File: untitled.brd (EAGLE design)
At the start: 59.4 x 57.8 mm, 25 parts

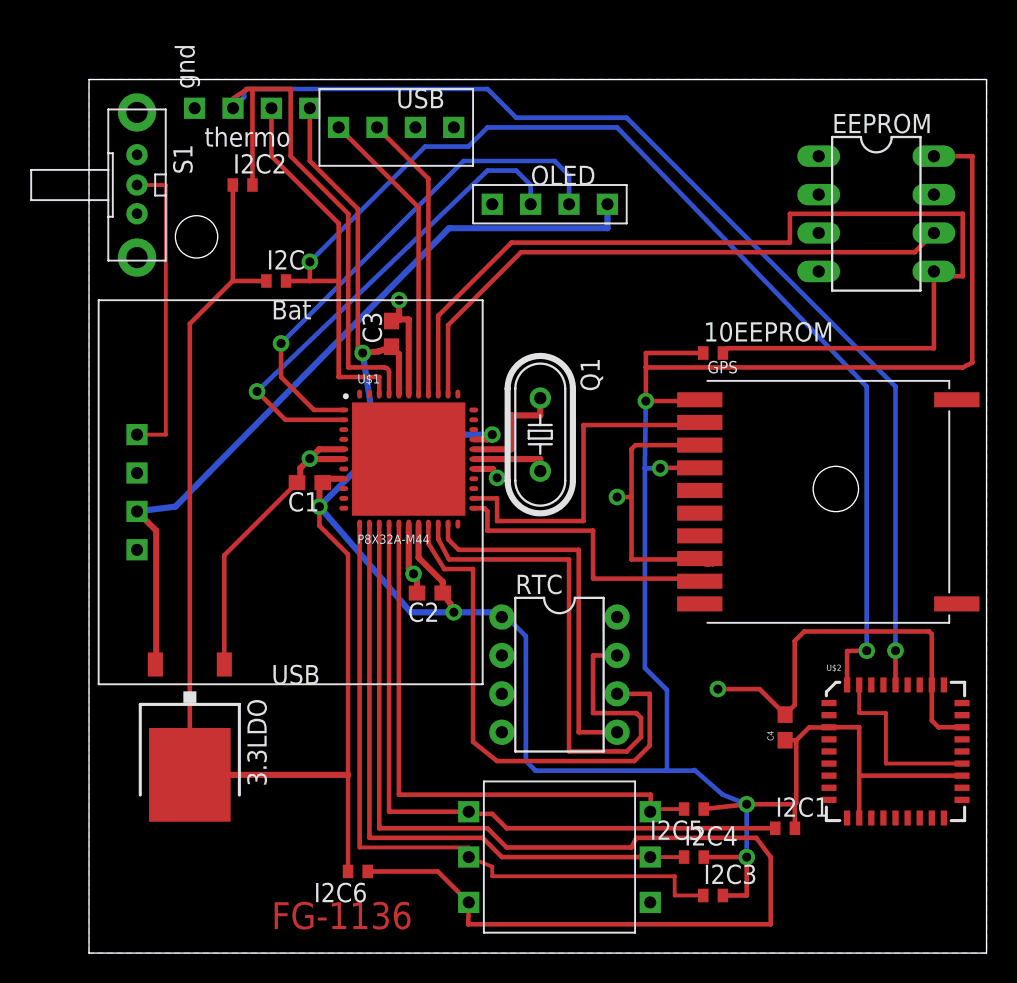
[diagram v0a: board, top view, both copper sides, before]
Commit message: Shrunk board form factor
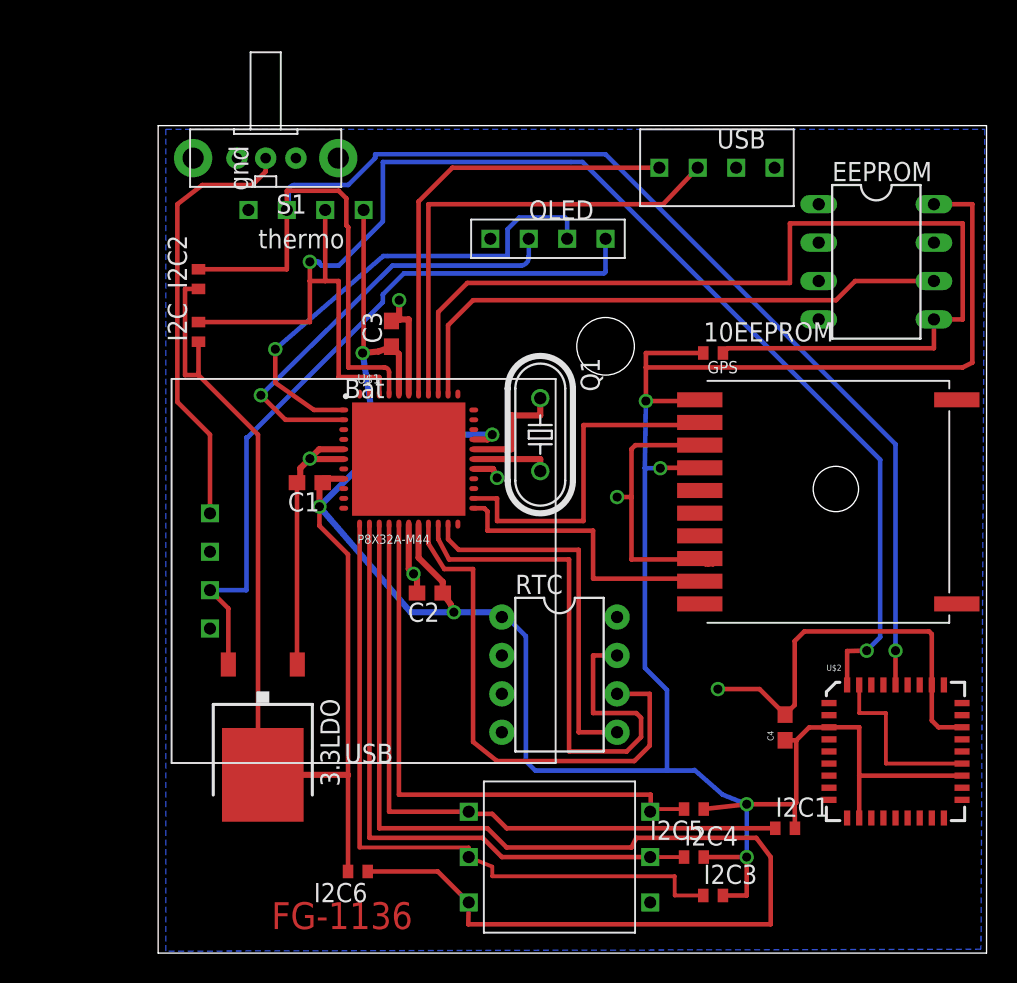
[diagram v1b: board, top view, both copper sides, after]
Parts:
- moved USB 21.4 mm to (75.2, 62.1)
- moved S1 8.69 mm to (45.3, 62.7), turned to 180 degrees
- moved THERMO 7.61 mm to (46.7, 59.3)
- moved LIPOCHARGER-BOOSTER 7.10 mm to (46.7, 36.7)
- moved I2C2 6.87 mm to (40.9, 54.7), turned to 90 degrees
- moved I2C 6.15 mm to (40.9, 51.2), turned to 90 degrees
- moved 3.3LDO 4.83 mm to (45.1, 24.4)
- moved EEPROM 3.17 mm to (85.7, 55.9)
- moved OLED_SCREEN 2.29 mm to (65.3, 57.4)
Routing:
- net +3V3: track 290.6 -> 270.1 mm
- net N$9: track 19.0 -> 31.4 mm
- net SCL: track 107.7 -> 97.2 mm
- net N$7: track 19.8 -> 29.6 mm
- net N$13: track 20.3 -> 28.9 mm
- net N$10: track 32.1 -> 28.8 mm
- net +5V: track 51.2 -> 48.7 mm
- net GND: track 82.1 -> 80.1 mm
- net N$19: track 39.2 -> 37.9 mm
- net N$11: track 33.6 -> 32.3 mm
- net SDA: track 97.0 -> 95.9 mm
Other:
- board size 59.4 x 57.8 mm -> 54.8 x 54.7 mm

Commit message: Made correction in hole size for through hole components
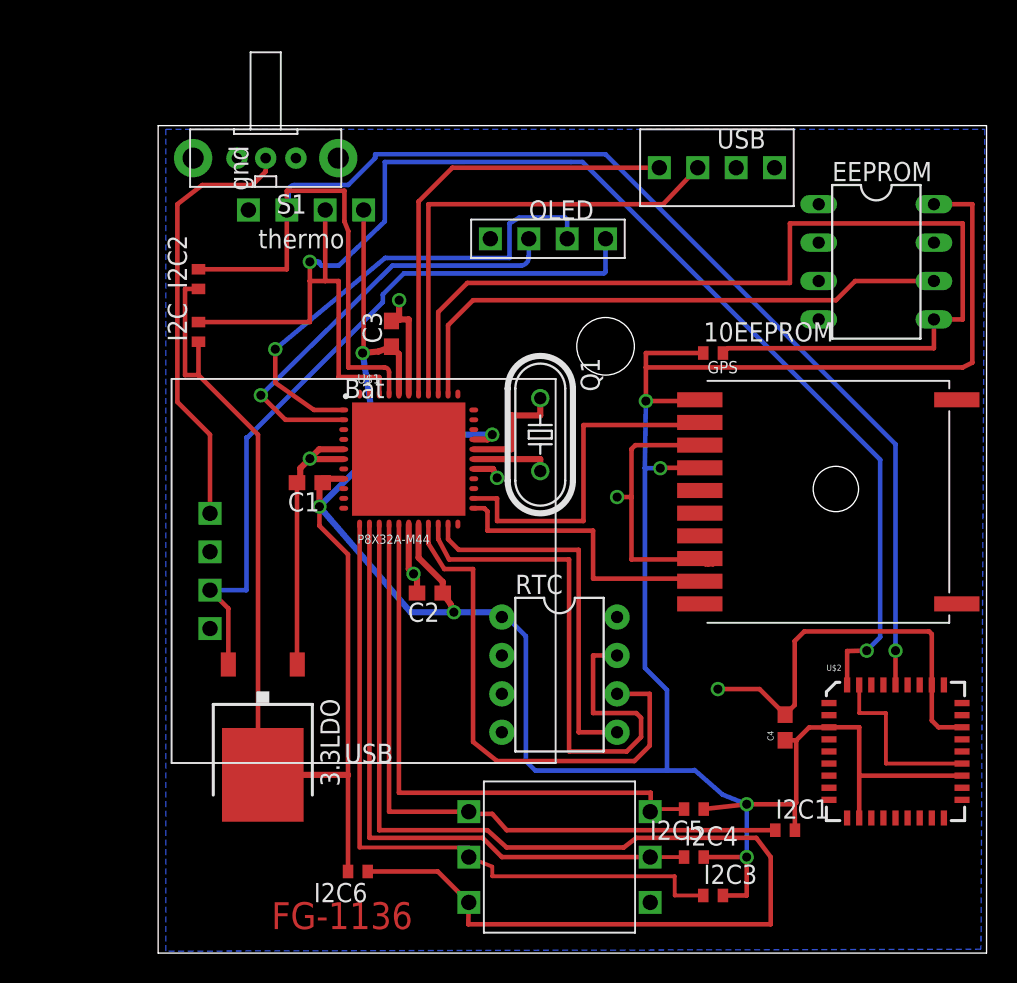
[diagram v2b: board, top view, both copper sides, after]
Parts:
- moved I2C1 0.13 mm to (79.7, 18.3)
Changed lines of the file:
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@@
 <element name="I2C3" library="adafruit" package="R1005" value="" x="74.93" y="13.97"/>
 <element name="I2C6" library="adafruit" package="R1005" value="" x="51.435" y="15.5575" rot="R180"/>
-<element name="I2C1" library="adafruit" package="R1005" value="" x="79.6925" y="18.415"/>
+<element name="I2C1" library="adafruit" package="R1005" value="" x="79.6925" y="18.288"/>
 <element name="U$2" library="SparkFun" package="LCC36" value="HMC6343A" x="86.995" y="23.495"/>
 <element name="C1" library="rcl" package="C0603" value="" x="48.26" y="41.275" rot="R180"/>
@@
 <wire x1="50.8" y1="48.895" x2="53.1825" y2="48.895" width="0.3048" layer="1"/>
 <wire x1="53.1825" y1="48.895" x2="53.5" y2="48.5775" width="0.3048" layer="1" curve="-90"/>
-<wire x1="50.165" y1="60.579" x2="46.736" y2="60.579" width="0.3048" layer="1"/>
+<wire x1="50.546" y1="60.579" x2="46.736" y2="60.579" width="0.3048" layer="1"/>
 <wire x1="46.736" y1="60.579" x2="46.736" y2="59.309" width="0.3048" layer="1"/>
 <wire x1="86.995" y1="43.815" x2="67.818" y2="62.992" width="0.3048" layer="16"/>
@@
 <wire x1="46.863" y1="60.579" x2="46.863" y2="59.436" width="0.3048" layer="16"/>
 <wire x1="46.863" y1="59.436" x2="46.736" y2="59.309" width="0.3048" layer="16" curve="-90"/>
-<wire x1="50.8" y1="48.895" x2="50.8" y2="58.166" width="0.3048" layer="1"/>
-<wire x1="50.8" y1="58.166" x2="50.673" y2="58.293" width="0.3048" layer="1"/>
-<wire x1="50.673" y1="58.293" x2="50.673" y2="60.071" width="0.3048" layer="1"/>
-<wire x1="50.165" y1="60.579" x2="50.673" y2="60.071" width="0.3048" layer="1"/>
+<wire x1="50.8" y1="48.895" x2="50.8" y2="57.912" width="0.3048" layer="1"/>
 <wire x1="40.894" y1="55.387" x2="46.736" y2="55.387" width="0.3048" layer="1"/>
 <wire x1="46.736" y1="55.387" x2="46.736" y2="59.309" width="0.3048" layer="1"/>
 <wire x1="86.995" y1="43.815" x2="86.995" y2="30.1625" width="0.3048" layer="16"/>
+<wire x1="50.546" y1="60.579" x2="50.546" y2="58.547" width="0.3048" layer="1"/>
+<wire x1="50.546" y1="58.547" x2="50.8" y2="57.912" width="0.3048" layer="1"/>
 </signal>
 <signal name="SDA">
@@
 <wire x1="83.795" y1="30.1375" x2="85.09" y2="30.1625" width="0.3048" layer="1"/>
 <via x="85.09" y="30.1625" extent="1-16" drill="0.6" shape="square"/>
-<wire x1="65.532" y1="62.484" x2="53.08980625" y2="62.4820625" width="0.3048" layer="16"/>
+<wire x1="65.532" y1="62.484" x2="53.21680625" y2="62.4820625" width="0.3048" layer="16"/>
 <via x="48.26" y="55.88" extent="1-16" drill="0.6" shape="square"/>
 <wire x1="48.26" y1="55.88" x2="48.26" y2="54.61" width="0.3048" layer="1"/>
@@
 <wire x1="65.532" y1="62.484" x2="66.294" y2="62.484" width="0.3048" layer="16"/>
 <wire x1="66.294" y1="62.484" x2="85.979" y2="42.799" width="0.3048" layer="16"/>
-<wire x1="53.08980625" y1="62.4820625" x2="53.08980625" y2="58.55080625" width="0.3048" layer="16"/>
-<wire x1="53.08980625" y1="58.55080625" x2="50.165" y2="55.626" width="0.3048" layer="16"/>
+<wire x1="53.21680625" y1="62.4820625" x2="53.21680625" y2="58.55080625" width="0.3048" layer="16"/>
+<wire x1="53.21680625" y1="58.55080625" x2="50.165" y2="55.626" width="0.3048" layer="16"/>
 <wire x1="50.165" y1="55.626" x2="49.022" y2="55.626" width="0.3048" layer="16"/>
 <wire x1="49.022" y1="55.626" x2="48.768" y2="55.88" width="0.3048" layer="16"/>
@@
 <contactref element="U$1" pad="1"/>
 <via x="45.974" y="50.1015" extent="1-16" drill="0.6" shape="square"/>
-<wire x1="53.11975" y1="56.2665625" x2="45.974" y2="50.1015" width="0.3048" layer="16"/>
+<wire x1="53.24675" y1="56.1395625" x2="45.974" y2="50.1015" width="0.3048" layer="16"/>
 <wire x1="50.5" y1="46.0813" x2="48.5337" y2="46.0813" width="0.3048" layer="1"/>
 <wire x1="48.5337" y1="46.0813" x2="45.974" y2="47.879" width="0.3048" layer="1"/>
@@
 <wire x1="65.278" y1="58.674" x2="65.151" y2="58.801" width="0.3048" layer="16"/>
 <wire x1="65.151" y1="58.801" x2="62.103" y2="58.801" width="0.3048" layer="16"/>
-<wire x1="62.103" y1="58.801" x2="61.341" y2="58.039" width="0.3048" layer="16"/>
-<wire x1="61.341" y1="58.039" x2="61.341" y2="56.261" width="0.3048" layer="16"/>
-<wire x1="61.341" y1="56.261" x2="53.3793125" y2="56.261" width="0.3048" layer="16"/>
-<wire x1="53.3793125" y1="56.261" x2="53.11975" y2="56.2665625" width="0.3048" layer="16"/>
+<wire x1="62.103" y1="58.801" x2="61.468" y2="58.42" width="0.3048" layer="16"/>
+<wire x1="61.468" y1="58.42" x2="61.468" y2="56.134" width="0.3048" layer="16"/>
+<wire x1="61.468" y1="56.134" x2="53.3793125" y2="56.134" width="0.3048" layer="16"/>
+<wire x1="53.3793125" y1="56.134" x2="53.24675" y2="56.1395625" width="0.3048" layer="16"/>
 </signal>
 <signal name="N$18">
@@
 <wire x1="53.5" y1="38.5313" x2="53.5" y2="19.51" width="0.3048" layer="1"/>
 <wire x1="53.5" y1="19.51" x2="58.77" y2="19.51" width="0.3048" layer="1"/>
-<wire x1="79.0425" y1="18.415" x2="61.2775" y2="18.415" width="0.3048" layer="1"/>
-<wire x1="61.2775" y1="18.415" x2="60.325" y2="19.3675" width="0.3048" layer="1"/>
+<wire x1="79.0425" y1="18.288" x2="61.2775" y2="18.288" width="0.3048" layer="1"/>
+<wire x1="61.2775" y1="18.288" x2="60.325" y2="19.3675" width="0.3048" layer="1"/>
 <wire x1="60.325" y1="19.3675" x2="58.9125" y2="19.3675" width="0.3048" layer="1"/>
 <wire x1="58.9125" y1="19.3675" x2="58.77" y2="19.51" width="0.3048" layer="1"/>
@@
 <contactref element="5WAYSWITCH" pad="D"/>
 <contactref element="I2C6" pad="1"/>
-<wire x1="52.85" y1="38.5313" x2="52.85" y2="18.415" width="0.3048" layer="1"/>
+<wire x1="52.85" y1="38.5313" x2="52.85" y2="18.288" width="0.3048" layer="1"/>
 <wire x1="77.7875" y1="17.78" x2="78.74" y2="16.51" width="0.3048" layer="1"/>
 <wire x1="78.74" y1="16.51" x2="78.74" y2="12.065" width="0.3048" layer="1"/>
 <wire x1="78.74" y1="12.065" x2="58.7375" y2="12.065" width="0.3048" layer="1"/>
 <wire x1="58.7375" y1="12.065" x2="58.77" y2="13.51" width="0.3048" layer="1"/>
-<wire x1="52.85" y1="18.415" x2="60.0075" y2="18.415" width="0.3048" layer="1"/>
-<wire x1="60.0075" y1="18.415" x2="61.2775" y2="17.145" width="0.3048" layer="1"/>
-<wire x1="61.2775" y1="17.145" x2="69.5325" y2="17.145" width="0.3048" layer="1"/>
+<wire x1="52.85" y1="18.288" x2="60.0075" y2="18.288" width="0.3048" layer="1"/>
+<wire x1="60.0075" y1="18.288" x2="61.2775" y2="17.145" width="0.3048" layer="1"/>
+<wire x1="61.2775" y1="17.145" x2="69.0245" y2="17.145" width="0.3048" layer="1"/>
 <wire x1="69.85" y1="17.78" x2="77.7875" y2="17.78" width="0.3048" layer="1"/>
 <wire x1="52.085" y1="15.5575" x2="56.7225" y2="15.5575" width="0.3048" layer="1"/>
 <wire x1="56.7225" y1="15.5575" x2="58.77" y2="13.51" width="0.3048" layer="1"/>
-<wire x1="69.85" y1="17.78" x2="69.5325" y2="17.145" width="0.3048" layer="1"/>
+<wire x1="69.85" y1="17.78" x2="69.0245" y2="17.145" width="0.3048" layer="1"/>
 </signal>
 <signal name="N$17">
@@
 <wire x1="73.01" y1="19.685" x2="70.77" y2="19.685" width="0.254" layer="1"/>
 <wire x1="70.77" y1="19.685" x2="70.77" y2="19.51" width="0.254" layer="1"/>
-<wire x1="54.15" y1="38.5313" x2="54.15" y2="20.6375" width="0.3048" layer="1"/>
-<wire x1="54.15" y1="20.6375" x2="70.8025" y2="20.6375" width="0.3048" layer="1"/>
-<wire x1="70.8025" y1="20.6375" x2="70.8025" y2="19.51" width="0.3048" layer="1"/>
+<wire x1="54.15" y1="38.5313" x2="54.15" y2="20.7645" width="0.3048" layer="1"/>
+<wire x1="54.15" y1="20.7645" x2="70.8025" y2="20.7645" width="0.3048" layer="1"/>
+<wire x1="70.8025" y1="20.7645" x2="70.8025" y2="19.51" width="0.3048" layer="1"/>
 <wire x1="70.8025" y1="19.51" x2="70.77" y2="19.51" width="0.3048" layer="1"/>
 </signal>
@@
 <wire x1="77.1525" y1="13.97" x2="77.1525" y2="16.51" width="0.3048" layer="1"/>
 <wire x1="77.1525" y1="20.0025" x2="80.3275" y2="20.0025" width="0.3048" layer="1"/>
-<wire x1="80.3275" y1="20.0025" x2="80.3425" y2="18.415" width="0.3048" layer="1"/>
+<wire x1="80.3275" y1="20.0025" x2="80.3425" y2="18.288" width="0.3048" layer="1"/>
 <wire x1="50.785" y1="15.5575" x2="50.785" y2="21.9075" width="0.3048" layer="1"/>
 <wire x1="50.785" y1="21.9475" x2="50.785" y2="36.5275" width="0.3048" layer="1"/>
@@
 <wire x1="51.816" y1="59.309" x2="51.816" y2="49.911" width="0.3048" layer="1"/>
 <wire x1="51.816" y1="49.911" x2="51.7525" y2="49.8475" width="0.3048" layer="1"/>
-<wire x1="40.894" y1="50.5945" x2="40.894" y2="48.514" width="0.3048" layer="1"/>
+<wire x1="40.894" y1="50.5945" x2="40.894" y2="48.387" width="0.3048" layer="1"/>
 <wire x1="40.894" y1="48.387" x2="44.831" y2="44.45" width="0.3048" layer="1"/>
 <wire x1="40.894" y1="54.087" x2="40.005" y2="54.087" width="0.3048" layer="1"/>
 <wire x1="40.005" y1="54.087" x2="40.005" y2="48.387" width="0.3048" layer="1"/>
 <wire x1="40.005" y1="48.387" x2="40.894" y2="48.387" width="0.3048" layer="1"/>
-<wire x1="40.894" y1="48.387" x2="40.894" y2="48.514" width="0.3048" layer="1"/>
 </signal>
 </signals>
